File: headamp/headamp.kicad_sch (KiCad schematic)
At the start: 77 parts, among them J1 MAINS 230V, K1 9V, SW1 ON/OFF, SW2 S2 wokal, SW202 S2 wokal (P), T1 OPT SE 5k:80R (>=25H, 45mA), T201 OPT SE 5k:80R (>=25H, 45mA), T301 EI84 100VA: 230V : 250V/0,15A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, U1 ECC82, U2 EL84 (trioda), U202 EL84 (trioda), U301 LD1085 (LDO)

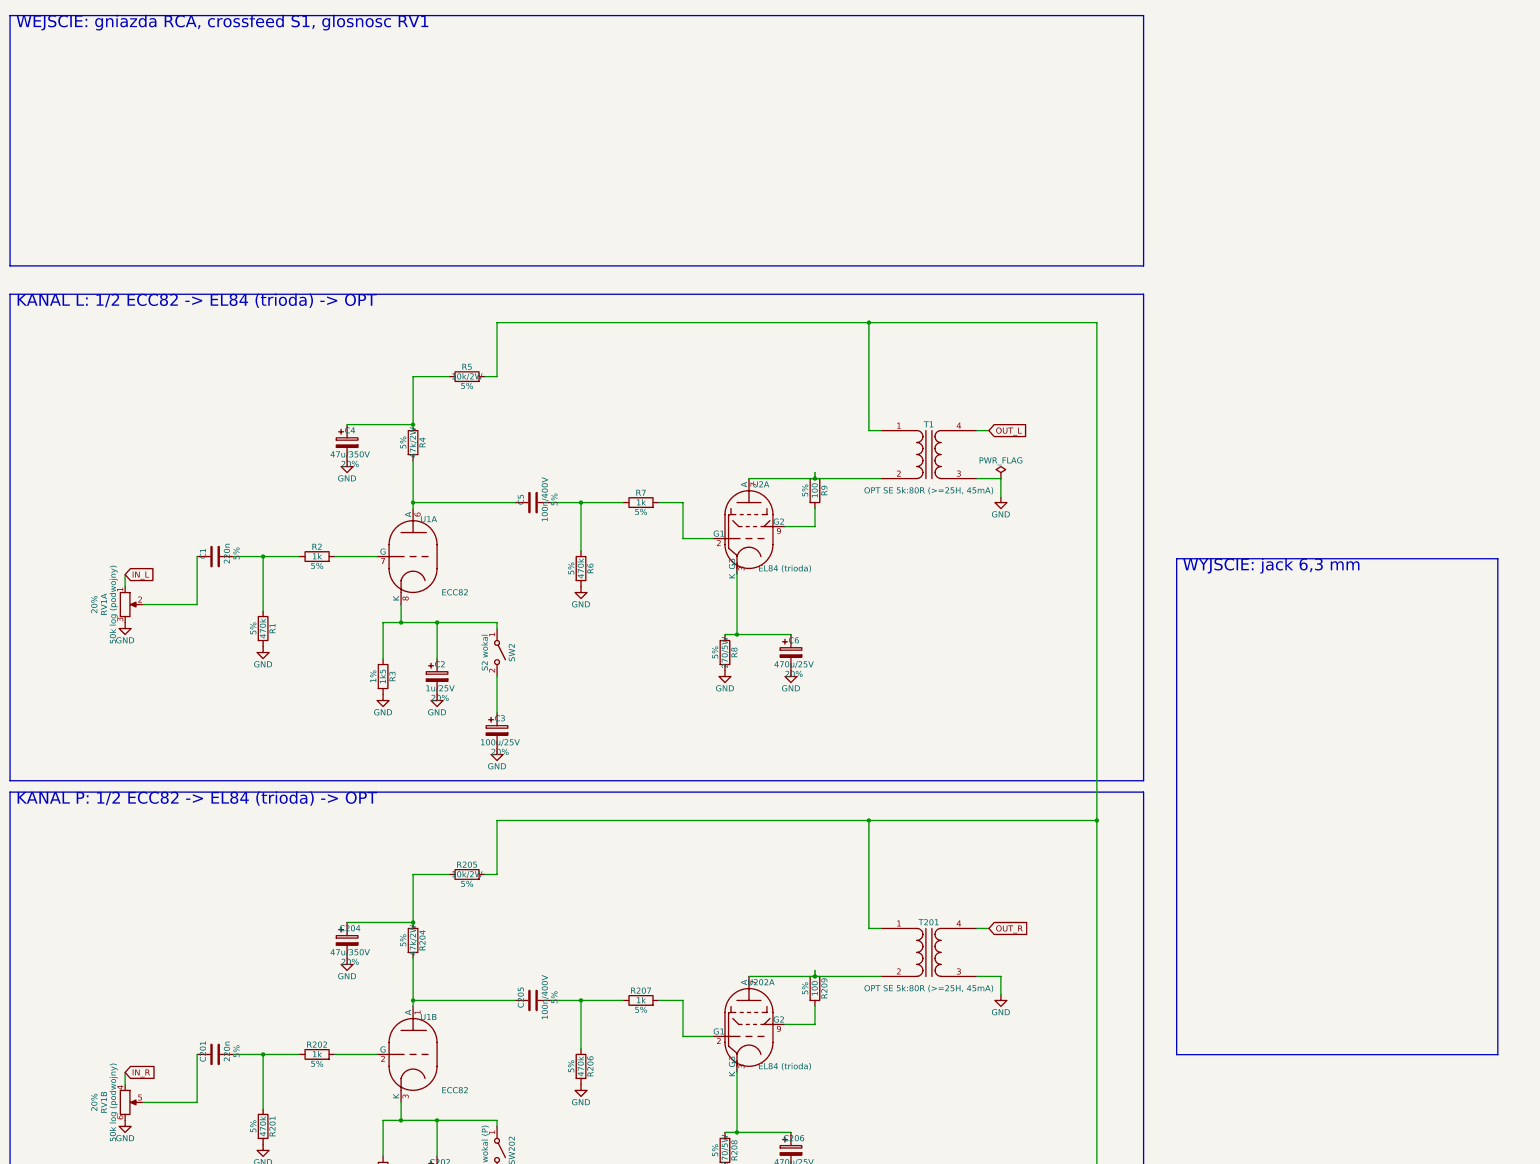
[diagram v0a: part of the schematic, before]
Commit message: headamp: crossfeed S1 (DPDT) + gniazda RCA/jack
Etap B (DECYZJE 2026-09-08):
- Crossfeed S1 (SW401, Switch:SW_DPDT_x2) miedzy gniazdami wejsciowymi a
  RV1. Topologia i wartosci - ZRODLO PRAWDY: headamp/sim/crossfeed.cir
  (bez przelacznika w cir - modeluje pozycje "krzyzowy" zalaczona). Tor
  prosty R401||C401 (kanal L), R402||C402 (kanal P) ZAWSZE wpiety miedzy
  gniazdo a RV1 (bypass przelacznika); SW401 przelacza tylko doplyw
  sygnalu do galezi krzyzowej (R403/C403/R405 L->P, R404/C404/R406 P->L,
  trzeci pin kazdego pola SW401 - NC = pozycja "prosty"). Numeracja 4xx
  (modul wejsciowy), jak ustalone.
- Gniazda wejsciowe J401/J402 (Connector:Conn_Coaxial, RCA) w module
  WEJSCIE; ekran -> GND.
- Gniazdo wyjsciowe J403 (Connector_Audio:AudioJack3, TRS 6,3mm) w module
  WYJSCIE: T=kanal L (T1 wtorne), R=kanal P (T201 wtorne), S=GND.
- IN_L/IN_R/OUT_L/OUT_R: global_label usuniete z chan() (Etap A zostawil
  je jako dangling do tego etapu) - teraz realne druty z WEJSCIE/WYJSCIE
  do odpowiednich pinow RV1/OPT (koniec hybrydy "druty zamiast etykiet").
- check.py: nowe asercje crossfeedu (gniazdo->SW401->tor prosty->RV1,
  galaz krzyzowa->C do masy->R do przeciwnego kanalu) i gniazd WY
  (T1.4/T201.4 -> J403 T/R, GND -> J403 S). Pozycji przelacznika (obu)
  nie da sie zweryfikowac statyczna netlista - udokumentowane w komentarzu.

ERC: 0 bledow oczekiwanych typem (missing_unit x3, multiple_net_names
ELEV/HEAT_B) + 3 bledy missing_power_pin (U1/U2/U202, patrz poprzedni
commit - konsekwencja braku unitow grzania, bez zmian w tym etapie).
Wszystkie warningi typu "isolated_pin_label"/"endpoint_off_grid" z tego
etapu wyeliminowane (gniazda/crossfeed domykaja IN/OUT, wspolrzedne na
siatce 1,27mm).

Co-Authored-By: Claude Sonnet 5 <noreply@anthropic.com>
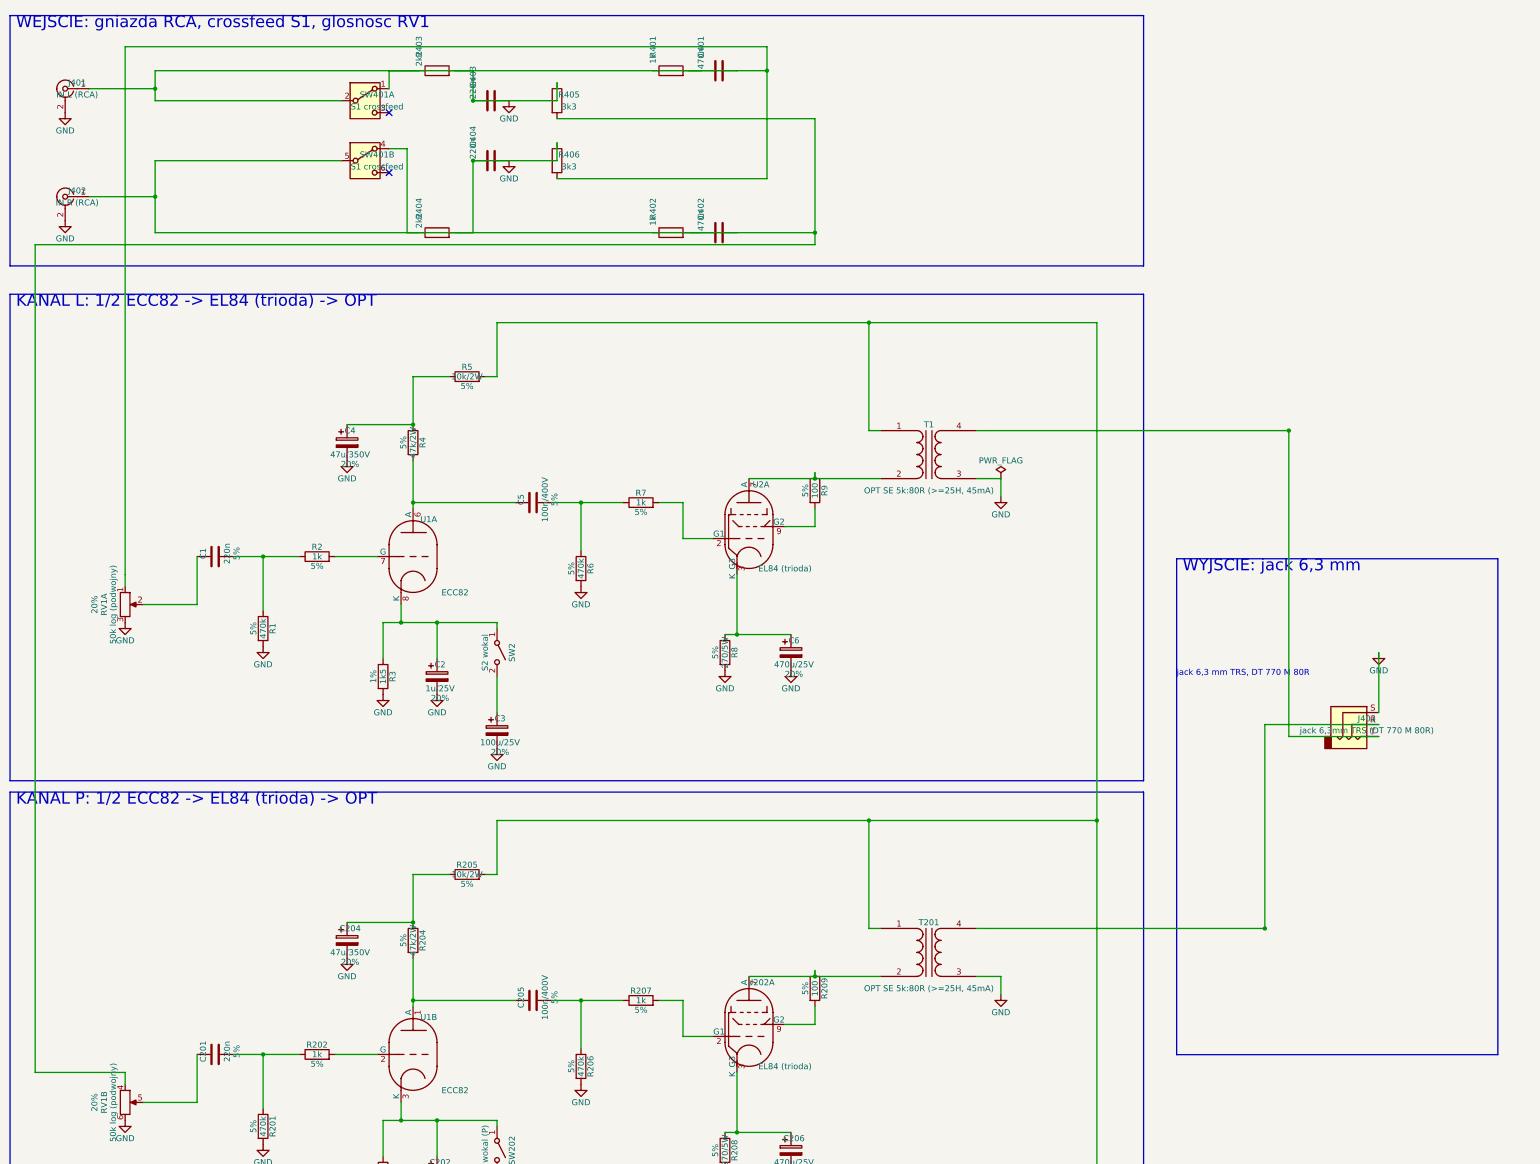
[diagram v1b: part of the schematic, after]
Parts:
- added C401, C402: 470n, symbol Device:C
- added C403, C404: 220n, symbol Device:C
- added J401: IN L (RCA), symbol Connector:Conn_Coaxial
- added J402: IN R (RCA), symbol Connector:Conn_Coaxial
- added J403: jack 6,3mm TRS (DT 770 M 80R), symbol Connector_Audio:AudioJack3
- added R401, R402: 1k, symbol Device:R
- added R403, R404: 2k2, symbol Device:R
- added R405, R406: 3k3, symbol Device:R
- added SW401: S1 crossfeed, symbol Switch:SW_DPDT_x2
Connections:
- net GND: now also C403.2, C404.2, J401.2 (Ext), J402.2 (Ext), J403.S
- net IN_L: no longer names the net of RV1.1
- net IN_L: now also C401.1, C401.2, C403.1, J401.1 (In), R401.1, R401.2, R403.1, R403.2, R405.1, R406.2, SW401.1 (A), SW401.2 (B)
- net IN_R: no longer names the net of RV1.4
- net IN_R: now also C402.1, C402.2, C404.1, J402.1 (In), R402.1, R402.2, R404.1, R404.2, R405.2, R406.1, SW401.4 (A), SW401.5 (B)
- net OUT_L: no longer names the net of T1.4 (SB)
- net OUT_L: now also J403.T
- net OUT_R: no longer names the net of T201.4 (SB)
- net OUT_R: now also J403.R
- no-connect marks 1 -> 3
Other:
- note added: "jack 6,3 mm TRS, DT 770 M 80R"

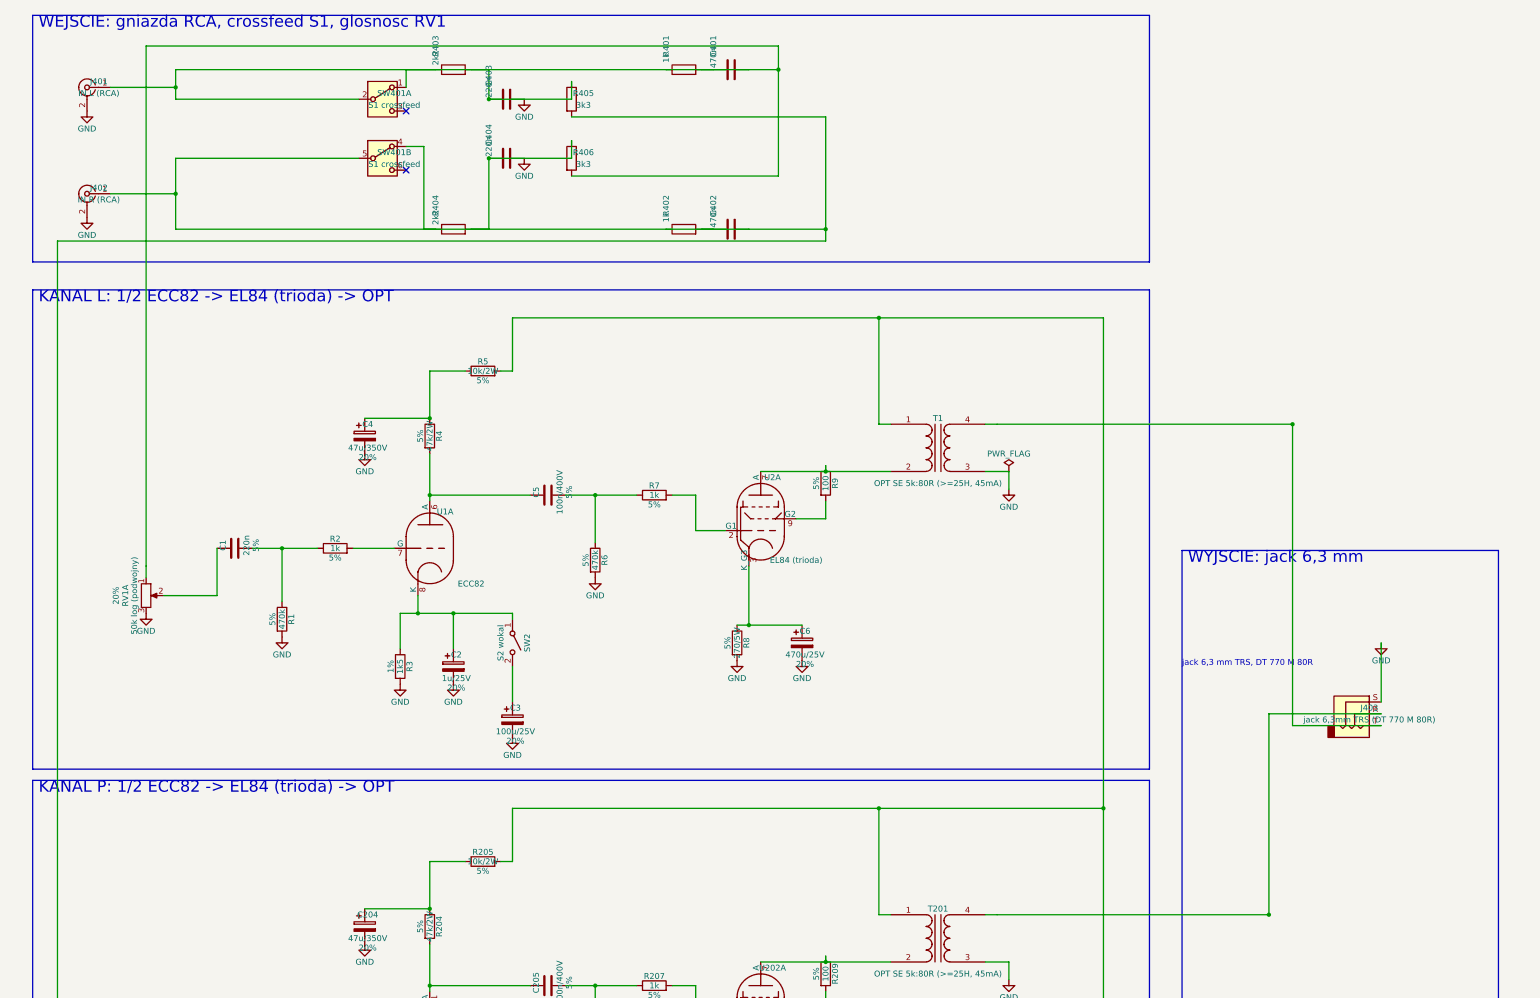
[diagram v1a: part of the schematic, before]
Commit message: headamp: przeglad koncowy - poprawki pol ref/value w module wejsciowym i J403
Etap D (przeglad PDF calosci + powiekszenia kazdego modulu):
- WEJSCIE: R401-R406/C401-C404 dostaly wlasne pola ref_at/val_at (wzor z
  chan()) - domyslne pozycje nachodzily sie przy kilku blisko postawionych
  rezystorach/kondensatorach. J401/J402 (gniazda RCA) przesuniete tak, zeby
  etykieta miescila sie w ramce modulu (wczesniej wystawala poza lewa
  krawedz).
- WYJSCIE: J403 przesuniete nizej w ramce + wlasne pola ref/value (domyslne
  nachodzily na sam symbol gniazda); usunieta zdublowana adnotacja
  tekstowa (ta sama tresc co pole Value).

Bez zmian topologii/wartosci - tylko kosmetyka. check.py OK (58 sieci),
ERC bez zmian (7 wpisow: missing_unit x3 + missing_power_pin x3 +
multiple_net_names ELEV/HEAT_B - jak w poprzednich commitach, patrz
docs/PROJEKT-HEADAMP.md TODO dla otwartej decyzji ws. missing_power_pin).

Co-Authored-By: Claude Sonnet 5 <noreply@anthropic.com>
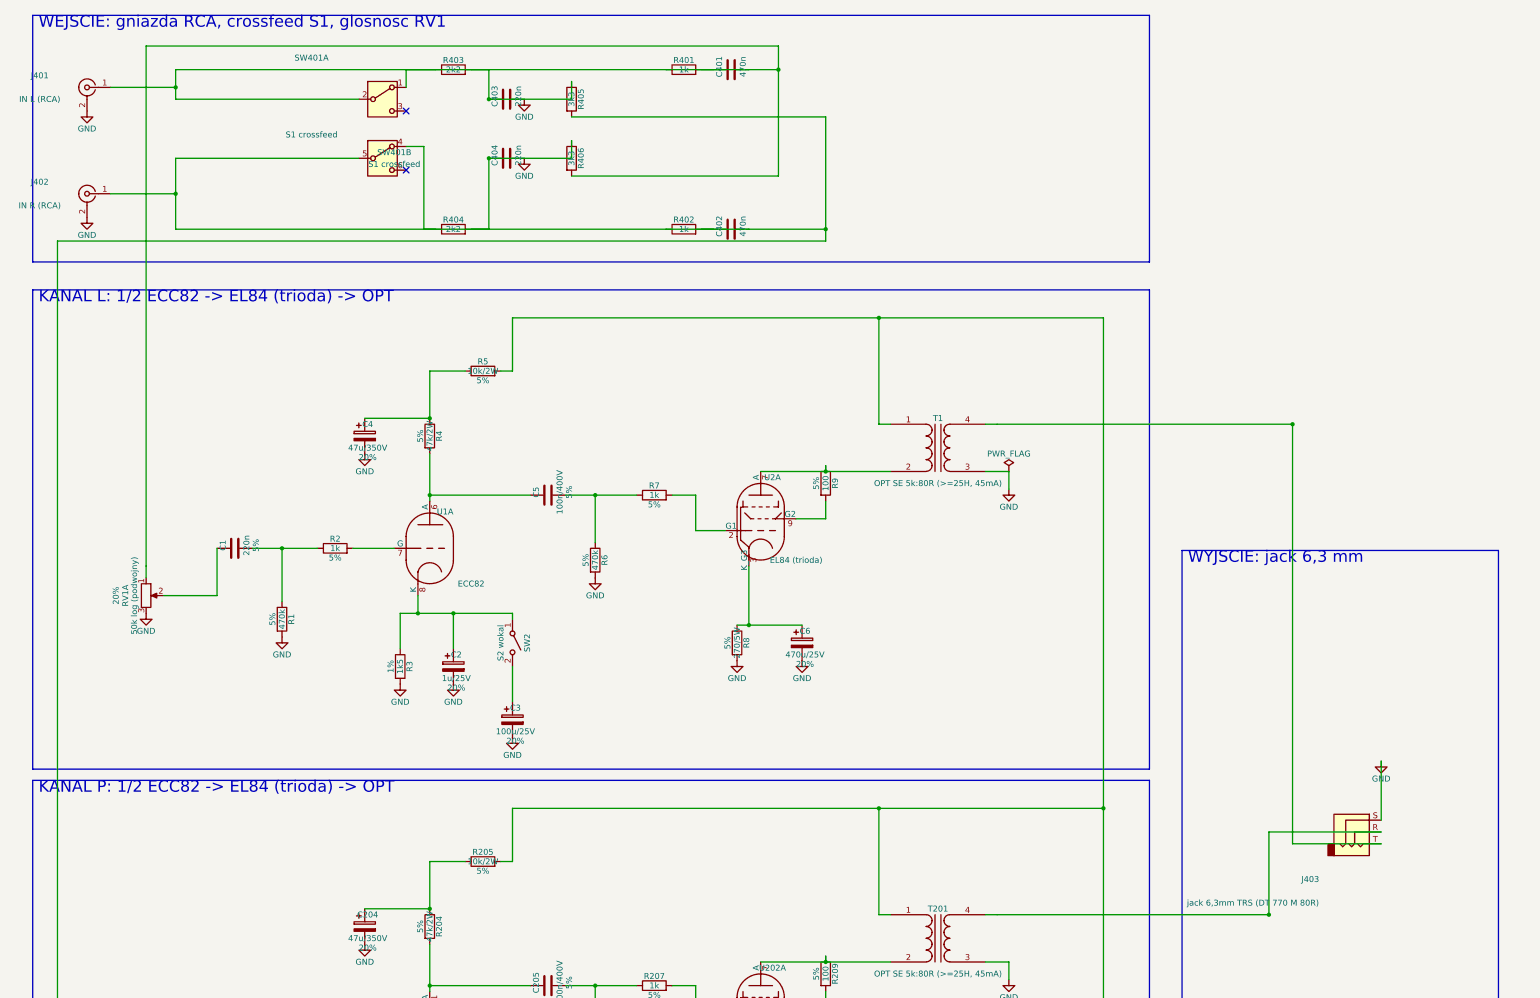
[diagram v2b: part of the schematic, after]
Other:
- note removed: "jack 6,3 mm TRS, DT 770 M 80R"
- moved on the sheet: J403

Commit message: headamp: zarniki lamp drutami w bloku zarzenia (ERC 0 bledow), prad zarzenia 1,7A, kosmetyka arkusza
Przywrocone (wariant a) unity grzania ECC82/EL84, rysowane realnymi
drutami wewnatrz ramki ZARZENIE zamiast etykiet HEAT_A/HEAT_B - usuwa
3 bledy missing_power_pin i 3 ostrzezenia missing_unit z ERC (teraz 0/0,
takze multiple_net_names ELEV/HEAT_B znika). Poprawiony blad w tekscie
na schemacie: prad zarzenia to ok. 1,7A (2x EL84 + ECC82), nie 0,3A.
Zmniejszony PSU_DY (26,67mm z 76,2mm) zamyka pusty pas miedzy KANAL P
a rzedem zasilacza; poszerzona ramka ZARZENIE pod trzy lampy. Dodane
asercje netlisty w check.py po stronie zarnikow.

Co-Authored-By: Claude Sonnet 5 <noreply@anthropic.com>
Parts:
- added unit 3 of U1
- added unit 2 of U2
- added unit 2 of U202
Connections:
- net ELEV: now also U1.9 (F2), U2.5 (F2), U202.5 (F2)
- net HEAT_A: no longer names the net of C308.1, R307.1, U301.2 (VO)
- net HEAT_A: now also U1.4 (F1), U1.5 (F1), U2.4 (F1), U202.4 (F1)
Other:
- note added: "LD1085 (LDO) - LM317 ma za duzy dropout przy 1,7A (V_RAW ~9V z uzwojenia 7V wystarcza)."
- note added: "Zarzenie do lamp: skrecona para, minus = ELEV (+53V)."
- note added: "Zarzenie: 6,3V DC / ok. 1,7A (2x EL84 0,76A + ECC82 0,15A; budzet 1,9A) z uzwojenia 7V/3A."
- note removed: "EL84 (x2) pin 4 -> HEAT_A, pin 5 -> HEAT_B. Zarniki NIE sa rysowane (patrz docs)."
- note removed: "Zarzenie do lamp (skrecona para): ECC82 piny 4+5 -> HEAT_A, pin 9 -> HEAT_B;"
- note removed: "Zarzenie: 6,3V DC / ok. 0,3A z uzwojenia 7V (3 lampy). LD1085 (LDO) - LM317 ma za duzy dropout."
- moved on the sheet: C301, C302, C303, C304, C305, C306, C307, C308, C309, D301, D302, D303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
